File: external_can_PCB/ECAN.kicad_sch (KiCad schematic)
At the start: 36 parts, among them J1 JST SH 4, J3 JST SH 6, J4 Micro_SD_Card, J5 JST SH 6, U1 SN65HVD232, U2 AP2127N-3.3, U3 TXB0104D, U5 STM32L562RETx, Y1 8 Mhz

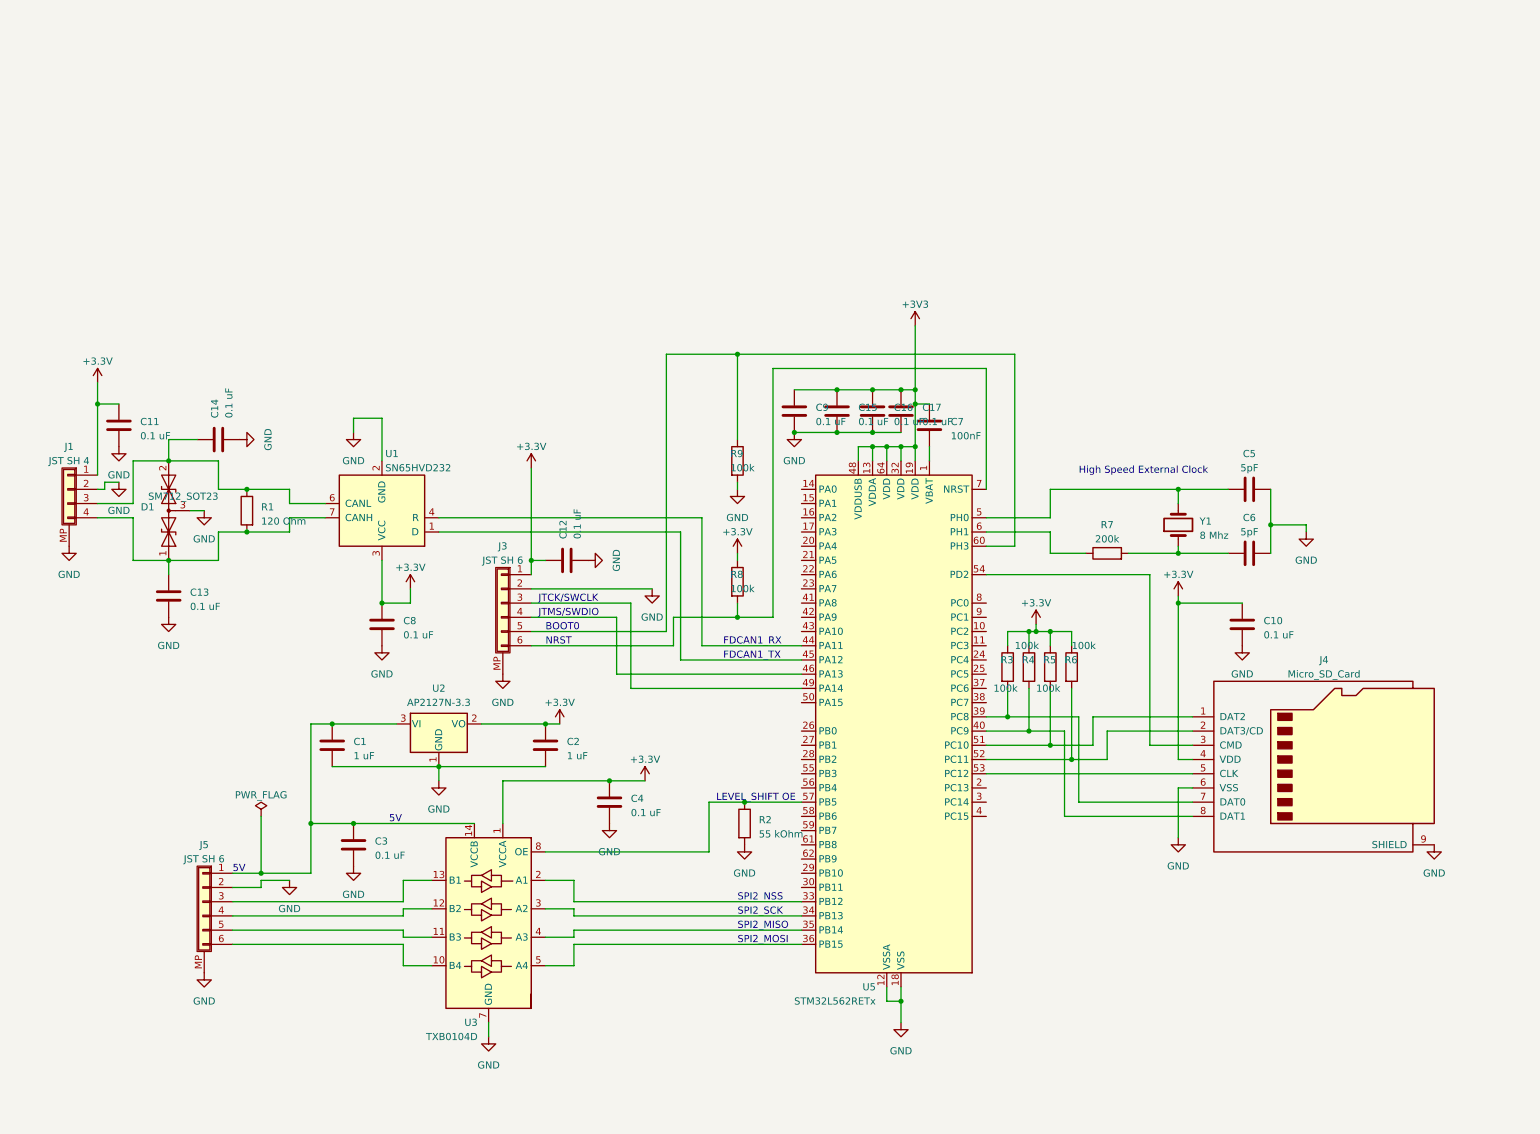
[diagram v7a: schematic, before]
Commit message: Redid ECAN Design: - Removed SPI Level Shifter * Changed JST SH Connector to JST GH * Cleaned up schematic
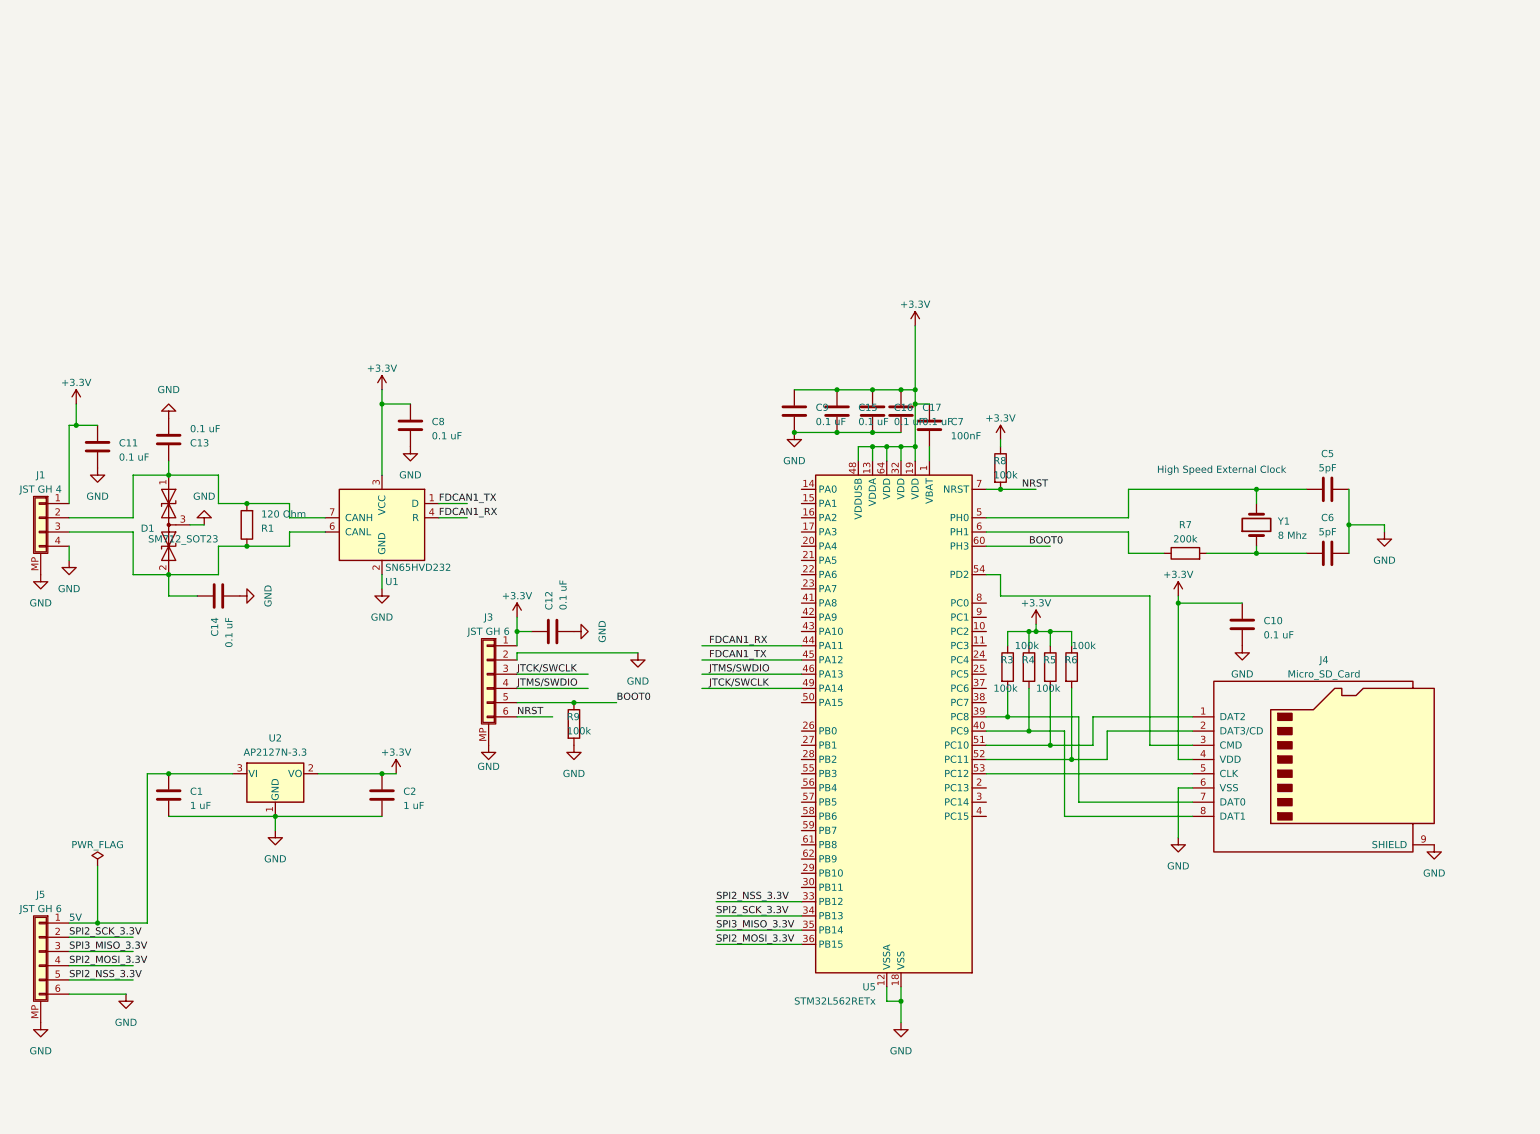
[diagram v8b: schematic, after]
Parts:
- removed C3, C4: 0.1 uF, Capacitor_SMD:C_0402_1005Metric_Pad0.74x0.62mm_HandSolder, symbol Device:C
- removed R2: 55 kOhm, Resistor_SMD:R_0402_1005Metric_Pad0.72x0.64mm_HandSolder, symbol Device:R
- removed U3: TXB0104D, Package_SO:SOIC-14_3.9x8.7mm_P1.27mm, symbol Logic_LevelTranslator:TXB0104D
- J1: value JST SH 4 -> JST GH 4; footprint Connector_JST:JST_SH_BM04B-SRSS-TB_1x04-1MP_P1.00mm_Vertical -> Connector_JST:JST_GH_SM04B-GHS-TB_1x04-1MP_P1.25mm_Horizontal
- J3, J5: value JST SH 6 -> JST GH 6; footprint Connector_JST:JST_SH_BM06B-SRSS-TB_1x06-1MP_P1.00mm_Vertical -> Connector_JST:JST_GH_SM06B-GHS-TB_1x06-1MP_P1.25mm_Horizontal
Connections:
- net +3V3 is gone; now on net +3.3V: C15.1, C16.1, C17.1, C7.2, C9.1, U5.13 (VDDA), U5.19 (VDD), U5.32 (VDD), U5.48 (VDDUSB), U5.64 (VDD)
- net GND: now also J1.4 (Pin_4), J5.6 (Pin_6); no longer J1.2 (Pin_2), J5.2 (Pin_2)
- net NRST: now reaches J3.6 (Pin_6), R8.2, U5.7 (NRST)
- net SPI2_NSS_3.3V: now reaches J5.5 (Pin_5)
- net SPI2_NSS_3.3V: now also U5.33 (PB12)
- net SPI2_MOSI_3.3V: now reaches J5.4 (Pin_4)
- net SPI2_MOSI_3.3V: now also U5.36 (PB15)
- net SPI3_MISO_3.3V: now reaches J5.3 (Pin_3)
- net SPI3_MISO_3.3V: now also U5.35 (PB14)
- net SPI2_SCK_3.3V: now reaches U5.34 (PB13)
- net SPI2_SCK_3.3V: now also J5.2 (Pin_2)
- net at C13.1, D1.1 (A1), R1.2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: now also J1.2 (Pin_2); no longer J1.4 (Pin_4)
- net FDCAN1_TX: now reaches U1.1 (D), U5.45 (PA12)
- net FDCAN1_RX: now reaches U1.4 (R), U5.44 (PA11)
- net JTMS/SWDIO: now reaches J3.4 (Pin_4), U5.46 (PA13)
- net JTCK/SWCLK: now reaches J3.3 (Pin_3), U5.49 (PA14)
- net BOOT0: now reaches J3.5 (Pin_5), R9.1, U5.60 (PH3)
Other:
- note removed: "BOOT0"
- note removed: "FDCAN1_RX"
- note removed: "FDCAN1_TX"
- note removed: "JTCK/SWCLK"
- note removed: "JTMS/SWDIO"
- note removed: "LEVEL_SHIFT OE"
- note removed: "NRST"
- note removed: "SPI2_MISO"
- note removed: "SPI2_MOSI"
- note removed: "SPI2_NSS"
- note removed: "SPI2_SCK"
- moved on the sheet: C1, C11, C12, C13, C14, C2, C5, C6, C8, D1, J1, J3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
